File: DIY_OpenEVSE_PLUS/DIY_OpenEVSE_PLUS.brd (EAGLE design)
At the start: 89.3 x 60.7 mm, 56 parts, among them IC1 AVR-MEGA8-PSIM, IC2 LF353, IC3 MID400, IC4 LM358, IC5 MID400, Q1 2N2222A, Q2 2N2222A, Y1 16000mhz

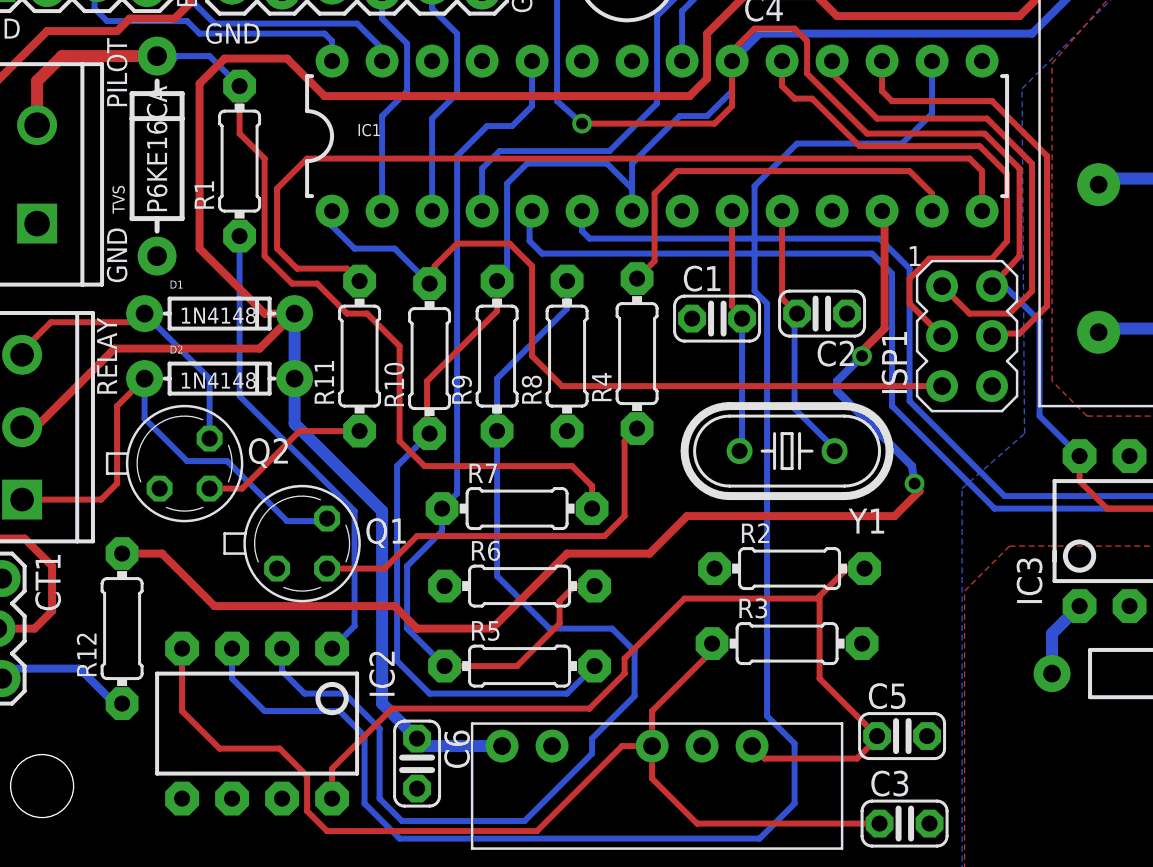
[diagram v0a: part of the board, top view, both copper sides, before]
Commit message: some airwire problems fix.
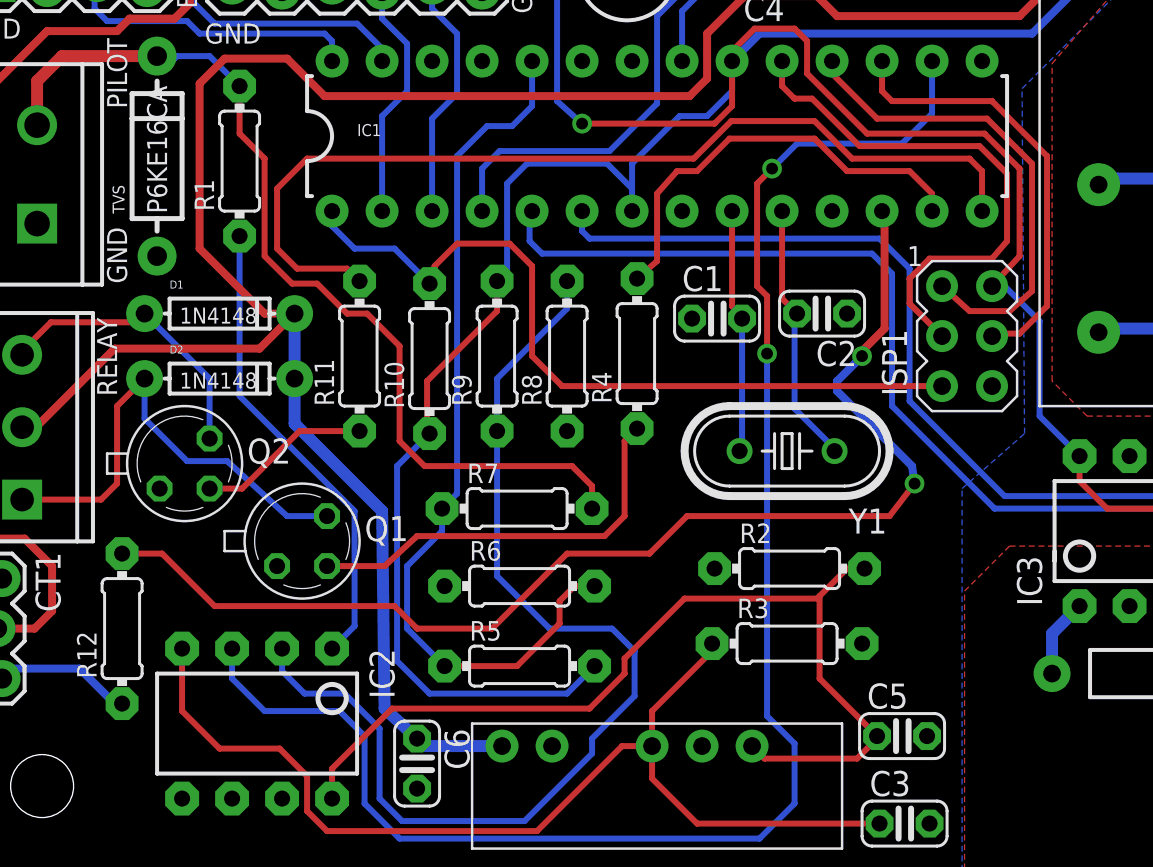
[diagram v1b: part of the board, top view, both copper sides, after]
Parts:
- moved Q1 0.13 mm to (17.7, 16.9)
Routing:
- net N$34: track 46.7 -> 48.2 mm
- net N$33: track 20.6 -> 22.0 mm
- net +12V: track 121.8 -> 122.3 mm
- net S$2: track 81.6 -> 81.5 mm, vias 0 -> 2
